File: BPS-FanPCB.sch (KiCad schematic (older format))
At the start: 21 parts, among them J1 LDRBRDConn, J2 FAN1, J3 FAN2, J4 FAN3, J5 FAN4, Q1 BUK9M34-100EX, Q2 BUK9M34-100EX, Q3 BUK9M34-100EX, Q4 BUK9M34-100EX

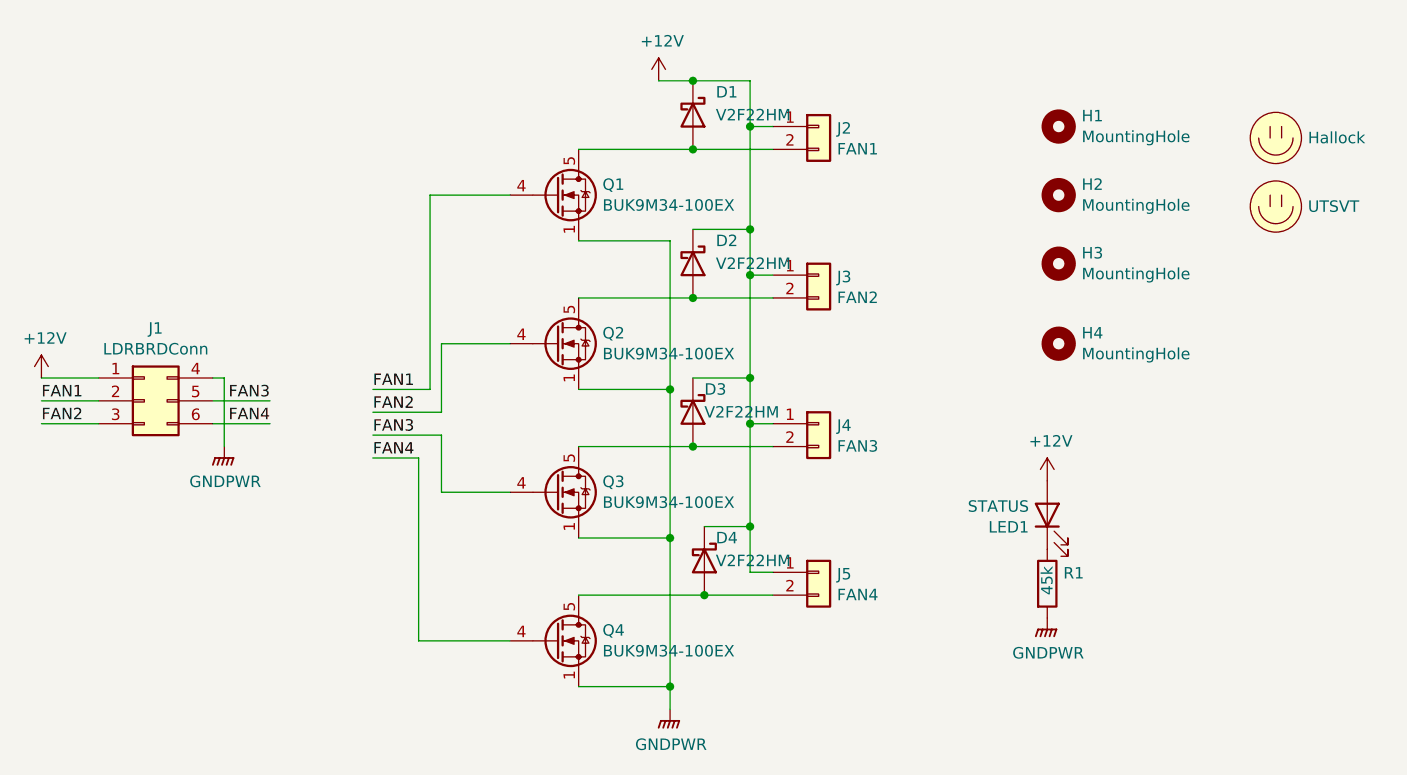
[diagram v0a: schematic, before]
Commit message: Renames kicad project to match repo
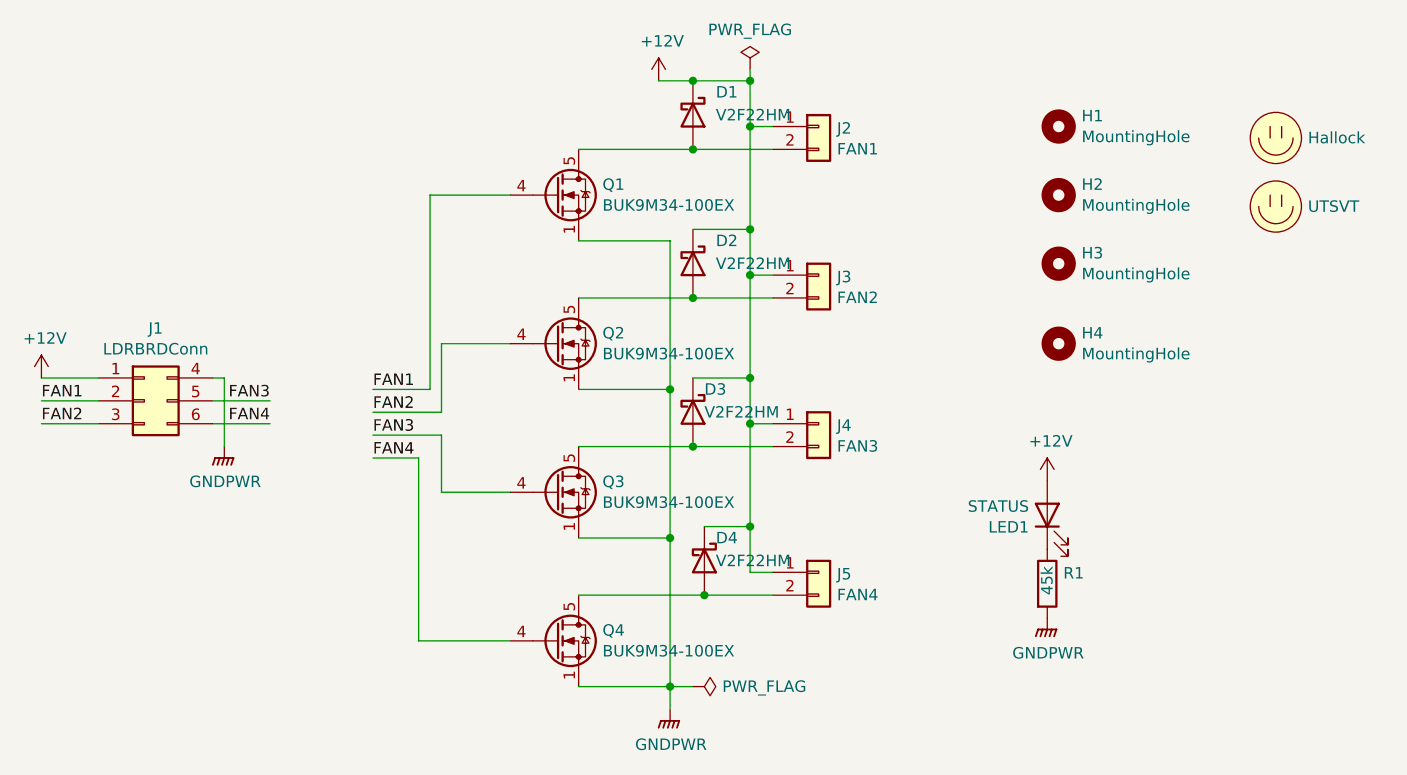
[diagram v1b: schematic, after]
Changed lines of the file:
@@
 	1    0    0    -1
 $EndComp
+$Comp
+L power:PWR_FLAG #FLG0101
+U 1 1 5F34F493
+P 3950 3400
+F 0 "#FLG0101" H 3950 3475 50  0001 C CNN
+F 1 "PWR_FLAG" H 3950 3573 50  0000 C CNN
+F 2 "" H 3950 3400 50  0001 C CNN
+F 3 "~" H 3950 3400 50  0001 C CNN
+	1    3950 3400
+	1    0    0    -1
+$EndComp
+Wire Wire Line
+	3950 3400 3950 3450
+Connection ~ 3950 3450
+$Comp
+L power:PWR_FLAG #FLG0102
+U 1 1 5F3510F0
+P 3700 6100
+F 0 "#FLG0102" H 3700 6175 50  0001 C CNN
+F 1 "PWR_FLAG" V 3700 6228 50  0000 L CNN
+F 2 "" H 3700 6100 50  0001 C CNN
+F 3 "~" H 3700 6100 50  0001 C CNN
+	1    3700 6100
+	0    1    1    0
+$EndComp
+Wire Wire Line
+	3600 6100 3700 6100
 $EndSCHEMATC
